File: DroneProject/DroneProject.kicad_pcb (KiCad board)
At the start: 4 copper layers, 100 x 100 mm, 327 parts, among them J21 Battery, J22 Debug, J23 UART, J24 Screw_Terminal_01x03, J25 Screw_Terminal_01x03, J26 Screw_Terminal_01x03, J27 Screw_Terminal_01x03, Q101 CSD17577Q5A, Q102 CSD17577Q5A, Q103 CSD17577Q5A, Q104 CSD17577Q5A, Q105 CSD17577Q5A, Q106 CSD17577Q5A, Q111 CSD17577Q5A, Q112 CSD17577Q5A, Q113 CSD17577Q5A, Q114 CSD17577Q5A, Q115 CSD17577Q5A, Q116 CSD17577Q5A, Q121 CSD17577Q5A, Q122 CSD17577Q5A, Q123 CSD17577Q5A, Q124 CSD17577Q5A, Q125 CSD17577Q5A, Q126 CSD17577Q5A, Q31 RJK0654DPB-00-J5, Q91 CSD17577Q5A, Q92 CSD17577Q5A, Q93 CSD17577Q5A, Q94 CSD17577Q5A, Q95 CSD17577Q5A, Q96 CSD17577Q5A, SW131 TS02CBE, SW31 PTS815 SJM 250 SMTR LFS, U101 DRV8320SRTVR, U102 INA180A2, U103 INA180A2, U111 DRV8320SRTVR, U112 INA180A2, U113 INA180A2, U121 DRV8320SRTVR, U122 INA180A2, U123 INA180A2, U131 NC7SZ04P5X, U132 TS3A4751PWR, U133 SN74LVC1G08DBVR, U134 TS3A4751PWR, U135 SN74LVC1G08DBVR, U136 TS3A4751PWR, U31 AP63203WU, U41 STM32F410RBT6, U61 LSM6DSOTR, U62 TMAG5273C1QDBVR, U63 INA181A1IDBVR, U64 M24C02-WMN6TP, U81 STM32G431RBTx, U91 DRV8320SRTVR, U92 INA180A2, U93 INA180A2

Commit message: Removed C1 and motor controllers from main platform and moved to own project
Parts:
- removed C101, C111, C121, C91: 10uF, Capacitor_SMD:C_1206_3216Metric
- removed C1010, C1012, C1013, C1014, C1015, C109, C1110, C1112, C1113, C1114, C1115, C119, C1210, C1212, C1213, C1214, C1215, C129, C910, C912, C913, C914, C915, C99: 1uF, Capacitor_SMD:C_0603_1608Metric
- removed C1011, C102, C108, C1111, C112, C118, C1211, C122, C128, C131, C133, C134, C814, C82, C83, C84, C85, C86, C911, C92, C98: 0.1uF, Capacitor_SMD:C_0402_1005Metric
- removed C103, C105, C113, C115, C123, C125, C813, C87, C93, C95: 1uF, Capacitor_SMD:C_0402_1005Metric
- removed C104, C114, C124, C94: 47nF, Capacitor_SMD:C_0402_1005Metric
- removed C106, C116, C126, C96: 440uF, Capacitor_THT:CP_Radial_D10.0mm_P5.00mm
- removed C81: 4.7uF, Capacitor_SMD:C_0805_2012Metric
- removed C810, C811, C812, C815, C816, C817, C818, C89: 1nf, Capacitor_SMD:C_0402_1005Metric
- removed C88: 10nF, Capacitor_SMD:C_0402_1005Metric
- removed D131: C1, LED_SMD:LED_0603_1608Metric
- removed D132: C0, LED_SMD:LED_0603_1608Metric
- removed FB81: FerriteBead, Inductor_SMD:L_0805_2012Metric
- removed NT10, NT101, NT102, NT111, NT112, NT12, NT121, NT122, NT2, NT4, NT6, NT8, NT91, NT92, NT93, NT94: NetTie_2, NetTie:NetTie-2_SMD_Pad0.5mm
- removed Q101, Q102, Q103, Q104, Q105, Q106, Q111, Q112, Q113, Q114, Q115, Q116, Q121, Q122, Q123, Q124, Q125, Q126, Q91, Q92, Q93, Q94, Q95, Q96: CSD17577Q5A, Package_TO_SOT_SMD:TDSON-8-1
- removed R101, R102, R103, R104, R105, R107, R111, R112, R113, R114, R115, R117, R121, R122, R123, R124, R125, R127, R131, R134, R135, R813, R818, R819, R823, R88, R91, R92, R93, R94, R95, R97: 10K, Resistor_SMD:R_0402_1005Metric
- removed R106, R116, R126, R416, R420, R424, R814, R815, R816, R817, R821, R822, R824, R85, R86, R87, R89, R96: 33, Resistor_SMD:R_0402_1005Metric
- removed R108, R109, R118, R119, R128, R129, R98, R99: CSS2H-2512K-2L00J, Resistor_SMD:R_2512_6332Metric
- removed R132, R133: 1K, Resistor_SMD:R_0402_1005Metric
- removed R81, R810, R811, R812, R82, R820, R83, R84: 100, Resistor_SMD:R_0402_1005Metric
- removed SW131: TS02CBE, Library:SW_TS02_10P16X5P08_CNK
- removed U101, U111, U121, U91: DRV8320SRTVR, Library:DRV8320SRTVR
- removed U102, U103, U112, U113, U122, U123, U92, U93: INA180A2, Package_TO_SOT_SMD:SOT-23-5
- removed U131: NC7SZ04P5X, Library:SC-88A-5_1P35X2P2_ONS
- removed U132, U134, U136: TS3A4751PWR, Library:SOP65P640X120-14N
- removed U133, U135: SN74LVC1G08DBVR, Library:SOT95P280X145-5N
- removed U81: STM32G431RBTx, Package_QFP:LQFP-64_10x10mm_P0.5mm
- added R35: Shunt, Resistor_SMD:R_2010_5025Metric, F.Cu at (383.6, 166.6)
- added U32: SN74LVC1G08DBVR, Library:SOT95P280X145-5N, F.Cu at (390.4, 166.7)
- R32: value 100 -> 10K; footprint Resistor_SMD:R_0201_0603Metric -> Resistor_SMD:R_0402_1005Metric
- R33: value 100K -> 100; footprint Resistor_SMD:R_0402_1005Metric -> Resistor_SMD:R_0201_0603Metric
- R34: value Shunt -> 100K; footprint Resistor_SMD:R_2010_5025Metric -> Resistor_SMD:R_0402_1005Metric
- moved SW31 290.1 mm to (398.2, 162.8), turned to 0 degrees
- moved C37 288.7 mm to (406.0, 149.4)
- moved R31 286.0 mm to (406.0, 139.5)
- moved C68 273.3 mm to (402.8, 126.8), turned to 0 degrees
- moved R417 271.1 mm to (390.0, 194.8)
- moved C43 270.8 mm to (396.6, 187.3), turned to 0 degrees
- moved R419 270.7 mm to (392.9, 188.8)
- moved R418 270.3 mm to (392.9, 186.8)
- moved R34 268.2 mm to (406.0, 143.5)
- moved C64 267.4 mm to (402.8, 122.9), turned to 0 degrees
- moved R414 267.1 mm to (390.0, 190.8)
- moved R413 266.9 mm to (390.0, 188.8)
- moved R64 266.1 mm to (399.9, 126.9), turned to 0 degrees
- moved NT31 265.6 mm to (401.3, 147.7), turned to 0 degrees
- moved R65 264.9 mm to (399.9, 128.9), turned to 0 degrees
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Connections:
- J24 pad 1: MTR1_A -> VDD
- J24 pad 2: MTR1_B -> MTR1_PWM
- J24 pad 3: MTR1_C -> GNDPWR
- J25 pad 1: MTR2_C -> VDD
- J25 pad 2: MTR2_B -> MTR2_PWM
- J25 pad 3: MTR2_A -> GNDPWR
- J26 pad 1: MTR3_A -> VDD
- J26 pad 2: MTR3_B -> MTR3_PWM
- J26 pad 3: MTR3_C -> GNDPWR
- J27 pad 1: MTR4_C -> VDD
- J27 pad 2: MTR4_B -> MTR4_PWM
- J27 pad 3: MTR4_A -> GNDPWR
- R32 pad 1: /Power/VBAT_SW -> GND
- R32 pad 2: /Power/VBAT_SW_R -> C0_NRST
- R33 pad 2: GND -> /Power/VBAT_SW_R
- R34 pad 1: +BATT -> /Power/VBAT_SW
- R34 pad 2: VDD -> GND
- R410 pad 1: C0_UART_TX -> UART_TX
- R413 pad 1: C0_SWDIO -> SWDIO
- R414 pad 1: C0_SWDIO -> SWDIO
- R415 pad 1: C0_SWCLK -> SWCLK
- R421 pad 1: C0_SWO -> SWO
- R422 pad 1: C0_SWO -> SWO
- R43 pad 1: C0_UART_RX -> UART_RX
- U41 pad 17: C0_UART_RX -> UART_RX
- U41 pad 26: Net-(U41B-PB0) -> unconnected-(U41B-PB0-Pad26)
- U41 pad 37: Net-(U41B-PC6) -> unconnected-(U41B-PC6-Pad37)
- U41 pad 43: Net-(U41B-PA10) -> unconnected-(U41B-PA10-Pad43)
- U41 pad 45: C0_SPI5_MISO -> unconnected-(U41B-PA12-Pad45)
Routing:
- net GND: track 263.4 -> 0.00 mm, vias 81 -> 0
- net +3.3V: track 213.2 -> 0.00 mm, vias 50 -> 0
- net C1_SPI2_MOSI: track 139.9 -> 0.00 mm, vias 10 -> 0
- net C1_SPI2_SCK: track 138.7 -> 0.00 mm, vias 10 -> 0
- net C1_SPI2_MISO: track 132.9 -> 0.00 mm, vias 7 -> 0
- net GNDPWR: track 107.3 -> 0.00 mm, vias 48 -> 0
- net C1_SWCLK: track 103.6 -> 0.00 mm, vias 7 -> 0
- net MTR3_CURR_A: track 101.2 -> 0.00 mm, vias 4 -> 0
- net C1_SWO: track 97.9 -> 0.00 mm, vias 3 -> 0
- net C1_SWDIO: track 96.4 -> 0.00 mm, vias 3 -> 0
- net /Prog/C0_SEL: track 91.1 -> 0.00 mm, vias 4 -> 0
- net /Prog/C1_SEL: track 78.3 -> 0.00 mm, vias 7 -> 0
- net C1_UART_RX: track 77.8 -> 0.00 mm, vias 3 -> 0
- net MTR1_CURR_A: track 68.4 -> 0.00 mm, vias 2 -> 0
- net MTR1_CURR_B: track 65.4 -> 0.00 mm, vias 4 -> 0
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- removed copper zone on In2.Cu, net +3.3V
- removed copper zone on F.Cu, net +BATT
- removed copper zone on In1.Cu, net GND
- removed copper zone on In1.Cu, net GNDPWR
- removed copper zone on B.Cu, net MTR1_A
- removed copper zone on F.Cu, net MTR1_A
- removed copper zone on B.Cu, net MTR1_B
- removed copper zone on F.Cu, net MTR1_B
- removed copper zone on B.Cu, net MTR1_C
- removed copper zone on F.Cu, net MTR1_C
- removed copper zone on B.Cu, net MTR2_A
- removed copper zone on F.Cu, net MTR2_A
- removed copper zone on B.Cu, net MTR2_B
- removed copper zone on F.Cu, net MTR2_B
- removed copper zone on B.Cu, net MTR2_C
- removed copper zone on F.Cu, net MTR2_C
- removed copper zone on B.Cu, net MTR3_A
- removed copper zone on F.Cu, net MTR3_A
- removed copper zone on B.Cu, net MTR3_B
- removed copper zone on F.Cu, net MTR3_B
- removed copper zone on B.Cu, net MTR3_C
- removed copper zone on F.Cu, net MTR3_C
- removed copper zone on B.Cu, net MTR4_A
- removed copper zone on F.Cu, net MTR4_A
- removed copper zone on B.Cu, net MTR4_B
- removed copper zone on F.Cu, net MTR4_B
- removed copper zone on B.Cu, net MTR4_C
- removed copper zone on F.Cu, net MTR4_C
- removed copper zone on F.Cu, net VDD
- removed copper zone on In2.Cu, net VDD
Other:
- board size 100 x 100 mm -> 60 x 100 mm
- board text removed: "C0 Active"
- board text removed: "C1 Active"
- board text removed: "Q31"

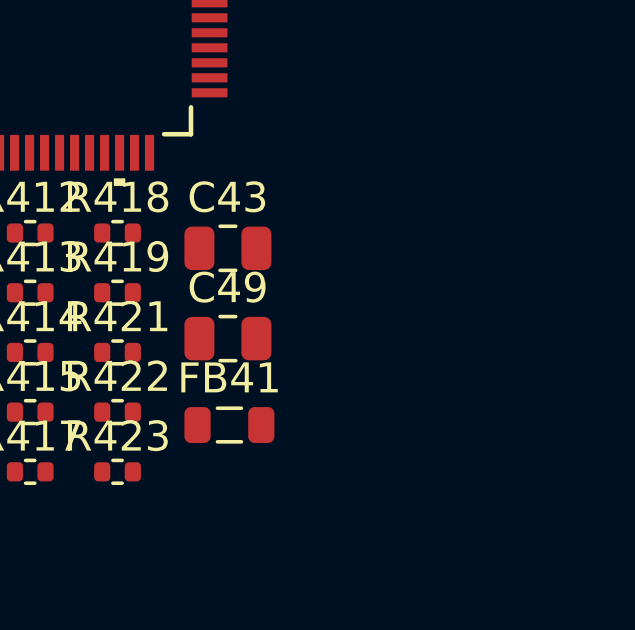
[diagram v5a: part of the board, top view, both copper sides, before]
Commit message: Completed schematic for brushless ESC and added needed components to main board.  The plan is to mount the ESCs on the main board using 2.54mm Vert Conn Headers
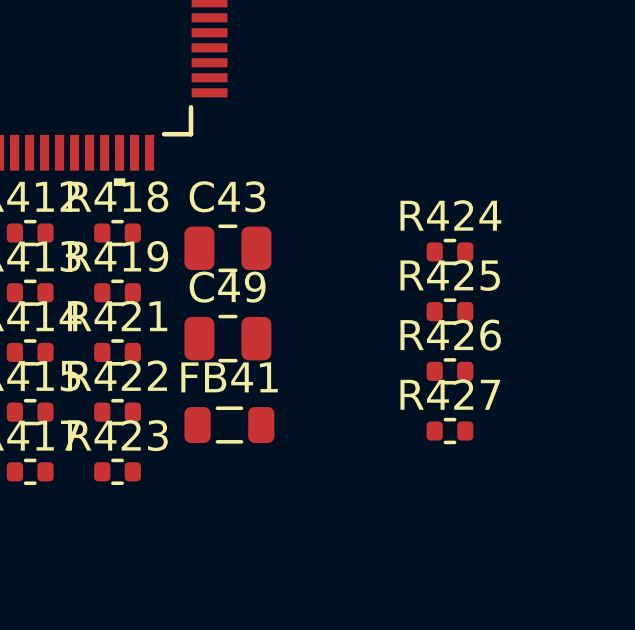
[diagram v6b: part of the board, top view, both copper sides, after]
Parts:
- added R424: 33, Resistor_SMD:R_0402_1005Metric, F.Cu at (404.0, 187.4)
- added R425: 33, Resistor_SMD:R_0402_1005Metric, F.Cu at (404.0, 189.4)
- added R426: 33, Resistor_SMD:R_0402_1005Metric, F.Cu at (404.0, 191.4)
- added R427: 33, Resistor_SMD:R_0402_1005Metric, F.Cu at (404.0, 193.4)
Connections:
- U41 pad 41: unconnected-(U41B-PA8-Pad41) -> Net-(U41B-PA8)
- U41 pad 42: unconnected-(U41B-PA9-Pad42) -> Net-(U41B-PA9)
- U41 pad 43: unconnected-(U41B-PA10-Pad43) -> Net-(U41B-PA10)
- U41 pad 44: unconnected-(U41B-PA11-Pad44) -> Net-(U41B-PA11)

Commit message: Finished layout for controller board
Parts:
- added C39: 470uF, Capacitor_SMD:CP_Elec_10x10.5, F.Cu at (150.3, 135.7)
- added R36: Shunt, Resistor_SMD:R_2010_5025Metric, F.Cu at (141.6, 132.6)
- added R428: 10K, Resistor_SMD:R_0402_1005Metric, F.Cu at (146.2, 112.2)
- added R429: 33, Resistor_SMD:R_0402_1005Metric, F.Cu at (148.7, 89.6)
- C38: value 470uF -> 0.1uF; footprint Capacitor_SMD:CP_Elec_10x10.5 -> Capacitor_SMD:C_0402_1005Metric
- J24, J25, J26, J27: value Screw_Terminal_01x03 -> ~; footprint Library:CUI_TB005_-762-03BE -> Library:BrushlessESC
- R33: value 100 -> 10K; footprint Resistor_SMD:R_0201_0603Metric -> Resistor_SMD:R_0402_1005Metric
- R34: value 100K -> 100; footprint Resistor_SMD:R_0402_1005Metric -> Resistor_SMD:R_0201_0603Metric
- R35: value Shunt -> 100K; footprint Resistor_SMD:R_2010_5025Metric -> Resistor_SMD:R_0402_1005Metric
- moved R71 315.9 mm to (117.6, 56.2), turned to 90 degrees
- moved R72 314.7 mm to (120.2, 56.2), turned to 90 degrees
- moved R73 313.4 mm to (122.8, 56.2), turned to 90 degrees
- moved D71 308.3 mm to (118.9, 56.3), turned to 90 degrees
- moved D72 307.4 mm to (121.5, 56.3), turned to 90 degrees
- moved D73 306.4 mm to (124.1, 56.3), turned to 90 degrees
- moved R32 283.3 mm to (124.3, 112.2), turned to 180 degrees
- moved R31 283.0 mm to (124.3, 113.2), turned to 180 degrees
- moved TP710 282.9 mm to (139.9, 87.4)
- moved C37 282.8 mm to (125.4, 114.2)
- moved TP711 280.3 mm to (141.2, 92.7)
- moved TP79 279.4 mm to (142.2, 90.6)
- moved TP78 279.3 mm to (135.8, 103.5)
- moved SW31 278.1 mm to (125.4, 108.7), turned to -90 degrees
- moved R427 278.1 mm to (141.3, 102.2)
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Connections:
- net Net-(U31-SW) renamed /Power/3.3_SW
- C38 pad 1: +BATT -> C0_NRST
- D71 pad 1: NRST -> C0_NRST
- J24 pad 1: VDD -> +3.3V
- J24 pad 2: MTR1_PWM -> GND
- J24 pad 3: GNDPWR -> MTR1_NRST
- J25 pad 1: VDD -> +3.3V
- J25 pad 2: MTR2_PWM -> GND
- J25 pad 3: GNDPWR -> MTR2_NRST
- J26 pad 1: VDD -> +3.3V
- J26 pad 2: MTR3_PWM -> GND
- J26 pad 3: GNDPWR -> MTR3_NRST
- J27 pad 1: VDD -> +3.3V
- J27 pad 2: MTR4_PWM -> GND
- J27 pad 3: GNDPWR -> MTR4_NRST
- R32 pad 1: GND -> SWD_NRST
- R32 pad 2: C0_NRST -> +3.3V
- R33 pad 1: /Power/VBAT_SW -> GND
- R33 pad 2: /Power/VBAT_SW_R -> C0_NRST
- R34 pad 2: GND -> /Power/VBAT_SW_R
- R35 pad 1: +BATT -> /Power/VBAT_SW
- R35 pad 2: VDD -> GND
- U41 pad 14: unconnected-(U41B-PA0-Pad14) -> MTR3_NRST
- U41 pad 15: unconnected-(U41B-PA1-Pad15) -> MTR3_FAULT
- U41 pad 25: TR_CE -> Net-(U41B-PC5)
- U41 pad 37: unconnected-(U41B-PC6-Pad37) -> MTR4_NRST
- U41 pad 38: unconnected-(U41B-PC7-Pad38) -> MTR4_FAULT
- U41 pad 52: unconnected-(U41B-PC11-Pad52) -> MTR2_NRST
- U41 pad 53: unconnected-(U41B-PC12-Pad53) -> MTR2_FAULT
- U41 pad 58: unconnected-(U41B-PB6-Pad58) -> MTR1_NRST
- U41 pad 59: unconnected-(U41B-PB7-Pad59) -> MTR1_FAULT
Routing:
- net GND: track 0.00 -> 273.6 mm, vias 0 -> 43
- net +3.3V: track 0.00 -> 173.1 mm, vias 0 -> 30
- net C0_NRST: track 0.00 -> 116.9 mm, vias 0 -> 4
- net MTR3_PWM: track 0.00 -> 75.7 mm, vias 0 -> 2
- net MTR2_FAULT: track 0.00 -> 74.6 mm, vias 0 -> 2
- net MTR1_PWM: track 0.00 -> 73.9 mm, vias 0 -> 2
- net ISEN_ADC: track 0.00 -> 70.2 mm, vias 0 -> 6
- net MTR2_PWM: track 0.00 -> 69.2 mm, vias 0 -> 2
- net MTR2_NRST: track 0.00 -> 68.7 mm, vias 0 -> 2
- net DBG_LED: track 0.00 -> 65.4 mm, vias 0 -> 2
- net MTR1_FAULT: track 0.00 -> 62.2 mm, vias 0 -> 2
- net TR_RXEN: track 0.00 -> 59.6 mm, vias 0 -> 4
- net UART_TX: track 0.00 -> 58.4 mm, vias 0 -> 3
- net MTR1_NRST: track 0.00 -> 58.0 mm, vias 0 -> 2
- net UART_RX: track 0.00 -> 56.0 mm, vias 0 -> 3
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- added copper zone on F.Cu, net +3.3V
- added copper zone on In2.Cu, net +3.3V
- added copper zone on F.Cu, net +BATT
- added copper zone on F.Cu, net -BATT
- added copper zone on F.Cu, net /Power/3.3_SW
- added copper zone on F.Cu, net /Power/VBAT_SW
- added copper zone on F.Cu, net GND
- added copper zone on In1.Cu, net GND
- added copper zone on In1.Cu, net GNDPWR
- added copper zone on F.Cu, net VBAT_TVS
- added copper zone on F.Cu, net VDD
- added copper zone on In2.Cu, net VDD
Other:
- board size 60 x 100 mm -> 80 x 100 mm
- board text added: "C0_I2C1_SCL"
- board text added: "C0_I2C1_SDA"
- board text added: "C0_SPI1_MISO"
- board text added: "C0_SPI1_MOSI"
- board text added: "C0_SPI1_SCK"
- board text added: "C0_SPI2_MISO"
- board text added: "C0_SPI2_MOSI"
- board text added: "C0_SPI2_SCK"
- board text added: "Debug"
- board text added: "IMU_CSN"
- board text added: "PWR_GOOD"
- board text added: "Reset"
- board text added: "TR_CSN"

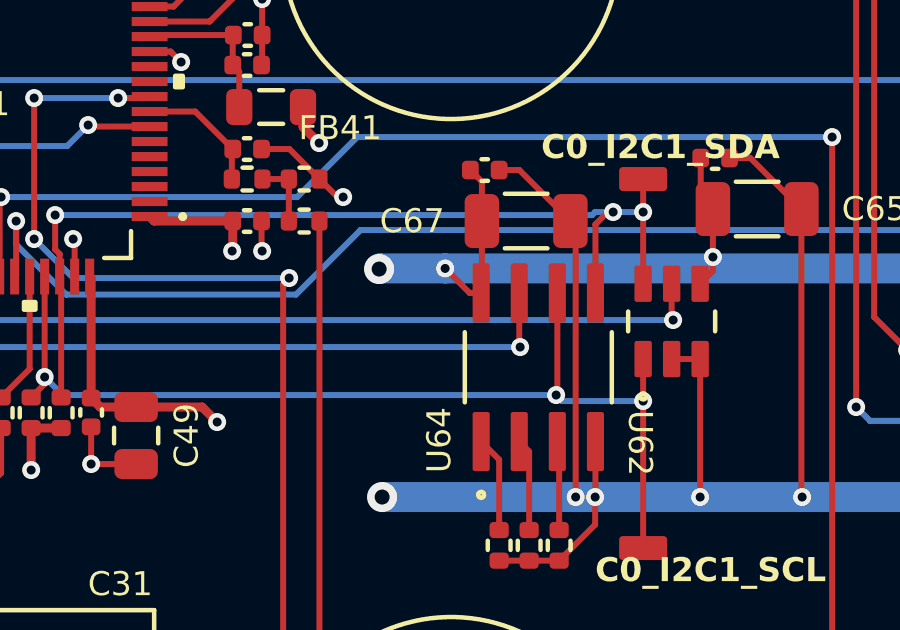
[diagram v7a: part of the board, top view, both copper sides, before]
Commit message: Finished brushless driver layout
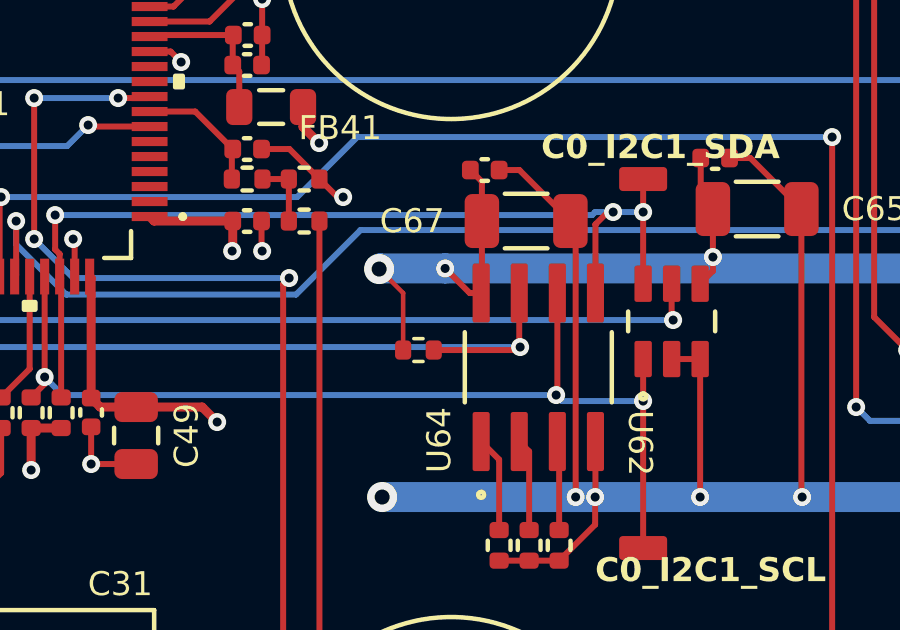
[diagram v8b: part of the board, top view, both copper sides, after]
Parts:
- added R67: 10K, Resistor_SMD:R_0402_1005Metric, F.Cu at (164.7, 108.2)
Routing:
- net +3.3V: track 173.1 -> 176.1 mm
- net EEPROM_WC: track 22.1 -> 25.0 mm
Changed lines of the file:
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@@
 		)
 	)
+	(footprint "Resistor_SMD:R_0402_1005Metric"
+		(layer "F.Cu")
+		(at 164.71 108.2 180)
+		(descr "Resistor SMD 0402 (1005 Metric), square (rectangular) end terminal, IPC-7351 nominal, (Body size source: IPC-SM-782 page 72, https://www.pcb-3d.com/wordpress/wp-content/uploads/ipc-sm-782a_amendment_1_and_2.pdf), generated with kicad-footprint-generator")
+		(tags "resistor")
+		(property "Reference" "R67"
+			(at 0 -1.17 0)
+			(layer "F.SilkS")
+			(hide yes)
+			(effects
+				(font
+					(size 1 1)
+					(thickness 0.15)
+				)
+			)
+		)
+		(property "Value" "10K"
+			(at 0 1.17 0)
+			(layer "F.Fab")
+			(effects
+				(font
+					(size 1 1)
+					(thickness 0.15)
+				)
+			)
+		)
+		(property "Datasheet" "~"
+			(at 0 0 0)
+			(layer "F.Fab")
+			(hide yes)
+			(effects
+				(font
+					(size 1.27 1.27)
+					(thickness 0.15)
+				)
+			)
+		)
+		(property "Description" "Resistor, US symbol"
+			(at 0 0 0)
+			(layer "F.Fab")
+			(hide yes)
+			(effects
+				(font
+					(size 1.27 1.27)
+					(thickness 0.15)
+				)
+			)
+		)
+		(property ki_fp_filters "R_*")
+		(sheetname "/Peripherals/")
+		(sheetfile "Sensors.kicad_sch")
+		(attr smd)
+		(fp_line
+			(start -0.153641 0.38)
+			(end 0.153641 0.38)
+			(stroke
+				(width 0.12)
+				(type solid)
+			)
+			(layer "F.SilkS")
+		)
+		(fp_line
+			(start -0.153641 -0.38)
+			(end 0.153641 -0.38)
+			(stroke
+				(width 0.12)
+				(type solid)
+			)
+			(layer "F.SilkS")
+		)
+		(fp_rect
+			(start -0.93 -0.47)
+			(end 0.93 0.47)
+			(stroke
+				(width 0.05)
+				(type solid)
+			)
+			(fill no)
+			(layer "F.CrtYd")
+		)
+		(fp_rect
+			(start -0.525 -0.27)
+			(end 0.525 0.27)
+			(stroke
+				(width 0.1)
+				(type solid)
+			)
+			(fill no)
+			(layer "F.Fab")
+		)
+		(fp_text user "${REFERENCE}"
+			(at 0 0 0)
+			(layer "F.Fab")
+			(effects
+				(font
+					(size 0.26 0.26)
+					(thickness 0.04)
+				)
+			)
+		)
+		(pad "1" smd roundrect
+			(at -0.51 0 180)
+			(size 0.54 0.64)
+			(layers "F.Cu" "F.Mask" "F.Paste")
+			(roundrect_rratio 0.25)
+			(net 59 "EEPROM_WC")
+			(pintype "passive")
+		)
+		(pad "2" smd roundrect
+			(at 0.51 0 180)
+			(size 0.54 0.64)
+			(layers "F.Cu" "F.Mask" "F.Paste")
+			(roundrect_rratio 0.25)
+			(net 4 "+3.3V")
+			(pintype "passive")
+		)
+		(embedded_fonts no)
+		(model "${KICAD9_3DMODEL_DIR}/Resistor_SMD.3dshapes/R_0402_1005Metric.step"
+			(offset
+				(xyz 0 0 0)
+			)
+			(scale
+				(xyz 1 1 1)
+			)
+			(rotate
+				(xyz 0 0 0)
+			)
+		)
+	)
 	(footprint "Capacitor_SMD:C_0402_1005Metric"
 		(layer "F.Cu")
@@
 	)
 	(segment
+		(start 164.2 108.2)
+		(end 164.2 106.3)
+		(width 0.1524)
+		(layer "F.Cu")
+		(net 4)
+	)
+	(segment
 		(start 135.3375 110.8)
 		(end 135.3375 112.5625)
@@
 	)
 	(segment
+		(start 164.2 106.3)
+		(end 163.4 105.5)
+		(width 0.1524)
+		(layer "F.Cu")
+		(net 4)
+	)
+	(segment
 		(start 136.2 133.541974)
 		(end 133.751 131.092974)
@@
 	)
 	(segment
+		(start 168.1 108.1)
+		(end 168 108.2)
+		(width 0.2)
+		(layer "F.Cu")
+		(net 59)
+	)
+	(segment
 		(start 150.25 108.05)
 		(end 150.25 105.749999)
@@
 		(width 0.2)
 		(layer "F.Cu")
+		(net 59)
+	)
+	(segment
+		(start 168 108.2)
+		(end 165.22 108.2)
+		(width 0.2)
+		(layer "F.Cu")
